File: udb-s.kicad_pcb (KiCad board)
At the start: 4 copper layers, 40 x 9 mm, 11 parts, among them J1 TYPE-C-31-M-12, J2 78171-0004, U1 TPD4E05U06DQAR

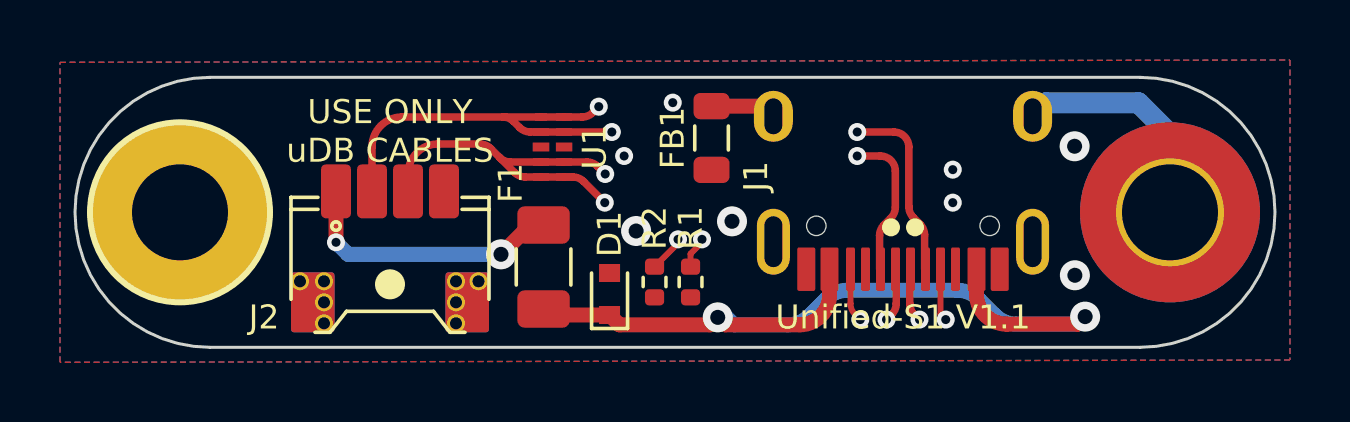
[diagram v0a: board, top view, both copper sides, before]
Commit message: Swap J2 Pico-EZmate for JST-SH compatible XYECONN XY-SH1.0-4A61
Same 1:1 pinout (5V, D-, D+, GND). Side-entry header sits where the
EZmate was, opening toward the board's inner edge. 5V/D-/D+ stubs
moved onto the 1.00 mm pins, F1's 5V via nudged 0.25 mm for clearance
to the new mounting pad, GND pour refilled. Files stay in KiCad 6
format.
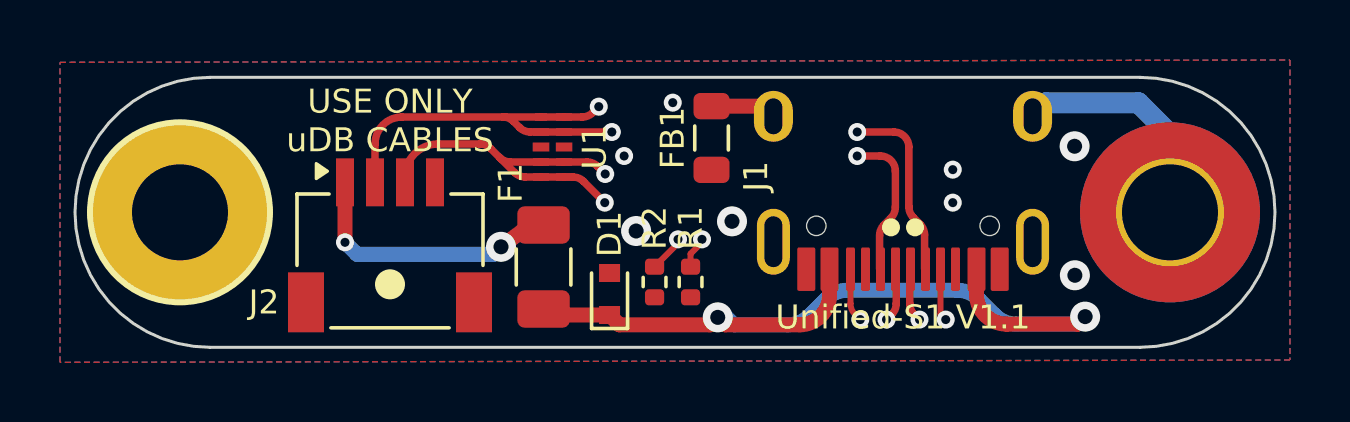
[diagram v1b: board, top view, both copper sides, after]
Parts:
- J2: value 78171-0004 -> XY-SH1.0-4A61; footprint locallib:PicoEZMate-Reinforced-Lite -> locallib:XY-SH1.0-4A61
- moved J2 0.50 mm to (122.0, 96.0)
